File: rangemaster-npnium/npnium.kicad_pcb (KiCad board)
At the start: 2 copper layers, 40 x 44 mm, 26 parts, among them J1 Conn_01x07_Male, Q1 Q_NPN_CBE

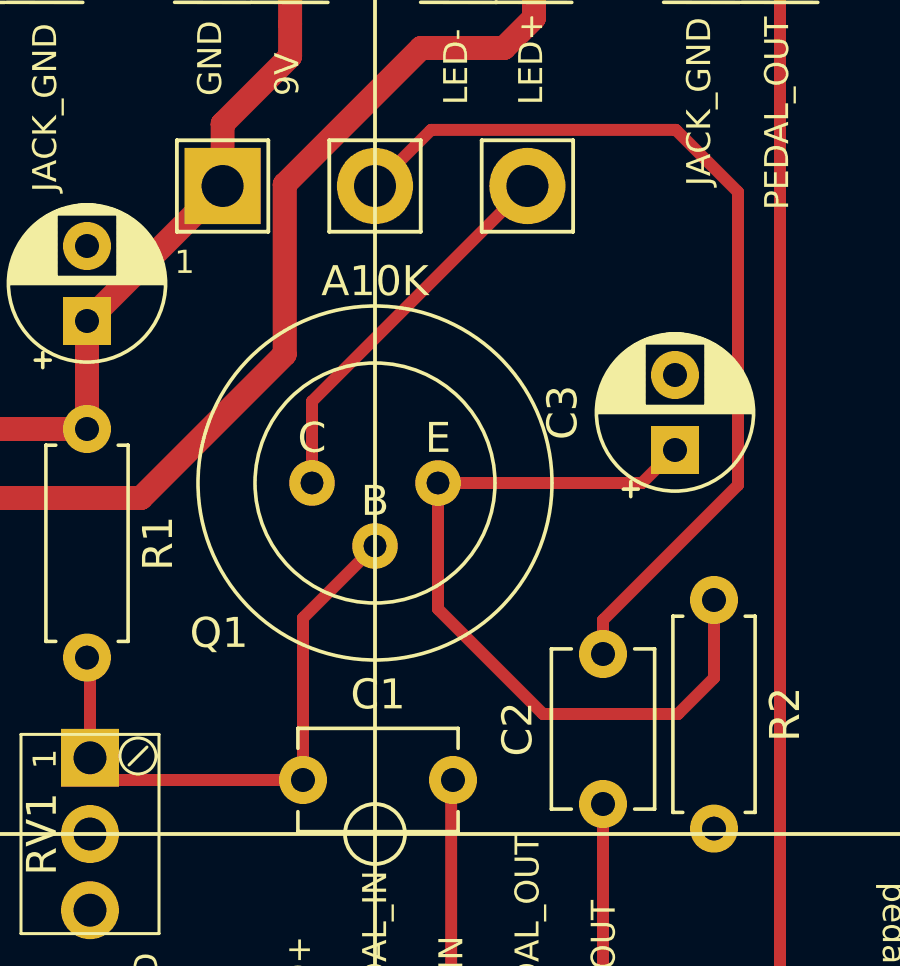
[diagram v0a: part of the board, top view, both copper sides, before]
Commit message: Migrating transistor footprint
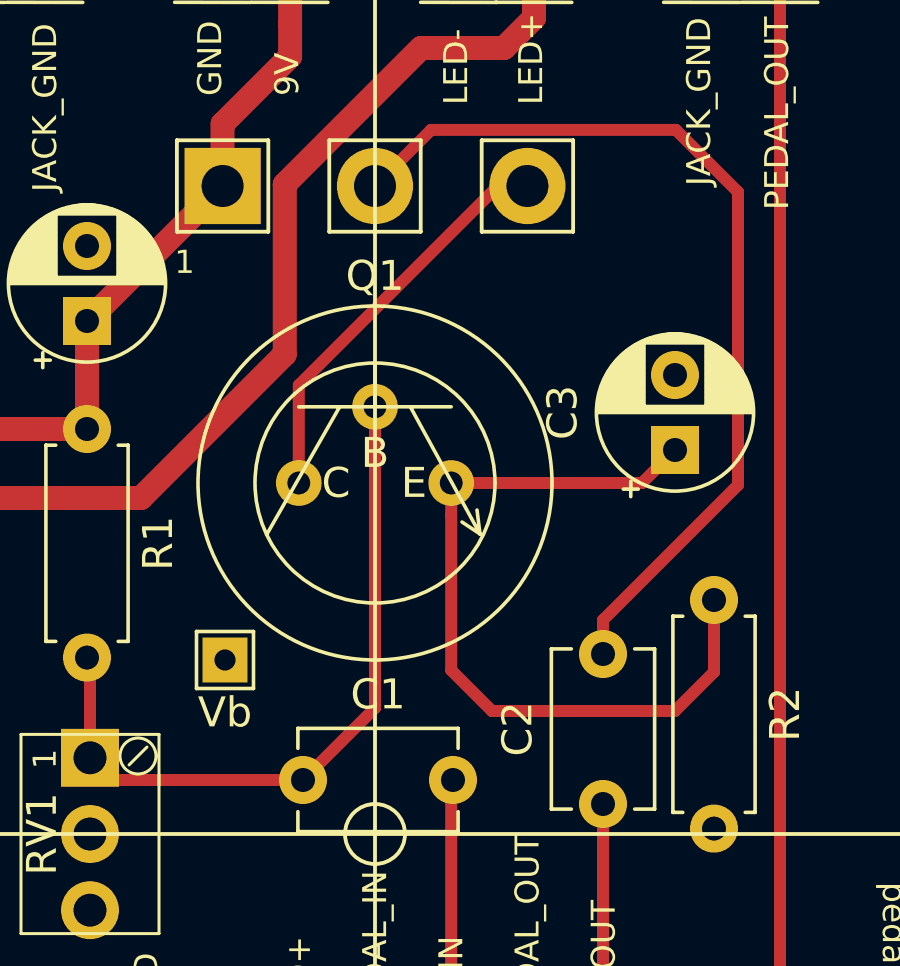
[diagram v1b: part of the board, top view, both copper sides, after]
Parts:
- added TP1: Vb, TestPoint:TestPoint_THTPad_1.5x1.5mm_Drill0.7mm, F.Cu at (95.0, 94.2)
- Q1: footprint pedal-component-footprint:Transistor_KTYU-3-6_CBE_d11.7mm -> pedal-component-footprint:Transistor_TO-5_CBE_d10.1mm
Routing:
- net Net-(C1-Pad1): track 19.6 -> 24.2 mm
- net Net-(Q1-Pad1): track 12.9 -> 13.6 mm
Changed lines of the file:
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@@
     (thickness 1.6)
     (drawings 10)
-    (tracks 66)
+    (tracks 67)
     (zones 0)
-    (modules 26)
+    (modules 27)
     (nets 12)
   )
@@
     (add_net "Net-(H6-Pad1)")
   )
+  (module TestPoint:TestPoint_THTPad_1.5x1.5mm_Drill0.7mm (layer F.Cu)
+    (at 95 94.2)
+    (descr "THT rectangular pad as test Point, square 1.5mm side length, hole diameter 0.7mm")
+    (tags "test point THT pad rectangle square")
+    (attr virtual)
+    (fp_text reference TP1 (at 0 -1.648) (layer F.SilkS) hide
+      (effects (font (size 1 1) (thickness 0.15)))
+    )
+    (fp_text value Vb (at 0 1.75) (layer F.SilkS)
+      (effects (font (size 1 1) (thickness 0.15)))
+    )
+    (fp_line (start 1.25 1.25) (end -1.25 1.25) (layer F.CrtYd) (width 0.05))
+    (fp_line (start 1.25 1.25) (end 1.25 -1.25) (layer F.CrtYd) (width 0.05))
+    (fp_line (start -1.25 -1.25) (end -1.25 1.25) (layer F.CrtYd) (width 0.05))
+    (fp_line (start -1.25 -1.25) (end 1.25 -1.25) (layer F.CrtYd) (width 0.05))
+    (fp_line (start -0.95 0.95) (end -0.95 -0.95) (layer F.SilkS) (width 0.12))
+    (fp_line (start 0.95 0.95) (end -0.95 0.95) (layer F.SilkS) (width 0.12))
+    (fp_line (start 0.95 -0.95) (end 0.95 0.95) (layer F.SilkS) (width 0.12))
+    (fp_line (start -0.95 -0.95) (end 0.95 -0.95) (layer F.SilkS) (width 0.12))
+    (fp_text user %R (at 0 -1.65) (layer F.Fab)
+      (effects (font (size 1 1) (thickness 0.15)))
+    )
+    (pad 1 thru_hole rect (at 0 0) (size 1.5 1.5) (drill 0.7) (layers *.Cu *.Mask)
+      (net 3 "Net-(C1-Pad1)"))
+  )
   (module "MBv3 enclosures:125B" (layer F.Cu)
     (at 100 100)
@@
     (fp_line (start 26 57.5) (end 0 57.5) (layer F.SilkS) (width 0.127))
   )
+  (module pedal-component-footprint:Transistor_TO-5_CBE_d10.1mm (layer F.Cu)
+    (at 100 88.3)
+    (fp_text reference Q1 (at 0 -6.9) (layer F.SilkS)
+      (effects (font (size 1 1) (thickness 0.15)))
+    )
+    (fp_text value Q_NPN_CBE (at 0 -6.8) (layer F.Fab)
+      (effects (font (size 1 1) (thickness 0.15)))
+    )
+    (fp_circle (center 0 0) (end 0 5.9) (layer F.SilkS) (width 0.12))
+    (fp_circle (center 0 0) (end 0 4) (layer F.SilkS) (width 0.12))
+    (fp_text user C (at -1.3 0) (layer F.SilkS)
+      (effects (font (size 1 1) (thickness 0.15)))
+    )
+    (fp_text user E (at 1.3 0) (layer F.SilkS)
+      (effects (font (size 1 1) (thickness 0.15)))
+    )
+    (fp_text user B (at 0 -1) (layer F.SilkS)
+      (effects (font (size 1 1) (thickness 0.15)))
+    )
+    (fp_line (start -2.54 -2.54) (end 2.54 -2.54) (layer F.SilkS) (width 0.12))
+    (fp_line (start -1.2 -2.5) (end -3.6 1.7) (layer F.SilkS) (width 0.12))
+    (fp_line (start 1.2 -2.5) (end 3.5 1.7) (layer F.SilkS) (width 0.12))
+    (fp_line (start 0 -2.6) (end 0 -4) (layer F.SilkS) (width 0.12))
+    (fp_line (start 3.5 1.7) (end 3.4 0.9) (layer F.SilkS) (width 0.12))
+    (fp_line (start 3.5 1.7) (end 2.9 1.3) (layer F.SilkS) (width 0.12))
+    (pad 1 thru_hole circle (at -2.54 0) (size 1.524 1.524) (drill 0.762) (layers *.Cu *.Mask)
+      (net 11 "Net-(Q1-Pad1)"))
+    (pad 2 thru_hole circle (at 0 -2.54) (size 1.524 1.524) (drill 0.762) (layers *.Cu *.Mask)
+      (net 3 "Net-(C1-Pad1)"))
+    (pad 3 thru_hole circle (at 2.54 0) (size 1.524 1.524) (drill 0.762) (layers *.Cu *.Mask)
+      (net 6 "Net-(C3-Pad1)"))
+  )
   (module pedal-component-footprint:PinHeader_1x01_P2.54mm_Long_Front_Back (layer F.Cu)
     (at 97.17 70.7)
@@
       (effects (font (size 1.2065 1.2065) (thickness 0.1524)) (justify mirror))
     )
-    (fp_text value A10K (at 0 -3.175) (layer F.SilkS)
+    (fp_text value A10K (at 0 2.9) (layer F.SilkS) hide
       (effects (font (size 1 1) (thickness 0.15)))
     )
@@
       (rotate (xyz 0 0 0))
     )
-  )
-  (module pedal-component-footprint:Transistor_KTYU-3-6_CBE_d11.7mm (layer F.Cu)
-    (at 100 88.3)
-    (fp_text reference Q1 (at -5.2 5) (layer F.SilkS)
-      (effects (font (size 1 1) (thickness 0.15)))
-    )
-    (fp_text value Q_NPN_CBE (at 0 -6.8) (layer F.Fab)
-      (effects (font (size 1 1) (thickness 0.15)))
-    )
-    (fp_text user E (at 2.1 -1.5) (layer F.SilkS)
-      (effects (font (size 1 1) (thickness 0.15)))
-    )
-    (fp_text user B (at 0 0.6) (layer F.SilkS)
-      (effects (font (size 1 1) (thickness 0.15)))
-    )
-    (fp_text user C (at -2.1 -1.5) (layer F.SilkS)
-      (effects (font (size 1 1) (thickness 0.15)))
-    )
-    (fp_circle (center 0 0) (end 0 5.9) (layer F.SilkS) (width 0.12))
-    (fp_circle (center 0 0) (end 0 4) (layer F.SilkS) (width 0.12))
-    (pad 1 thru_hole circle (at -2.1 0) (size 1.524 1.524) (drill 0.762) (layers *.Cu *.Mask)
-      (net 11 "Net-(Q1-Pad1)"))
-    (pad 2 thru_hole circle (at 0 2.1) (size 1.524 1.524) (drill 0.762) (layers *.Cu *.Mask)
-      (net 3 "Net-(C1-Pad1)"))
-    (pad 3 thru_hole circle (at 2.1 0) (size 1.524 1.524) (drill 0.762) (layers *.Cu *.Mask)
-      (net 6 "Net-(C3-Pad1)"))
   )
   (module pedal-component-footprint:BoardHeader_1x07_P2.54mm_Long_FXSide (layer F.Cu)
@@
   (segment (start 90.5 94.22) (end 90.4 94.12) (width 0.4) (layer F.Cu) (net 3))
   (segment (start 90.5 97.46) (end 90.5 94.22) (width 0.4) (layer F.Cu) (net 3))
-  (segment (start 97.6 92.8) (end 100 90.4) (width 0.4) (layer F.Cu) (net 3))
-  (segment (start 97.6 98.2) (end 97.6 92.8) (width 0.4) (layer F.Cu) (net 3))
+  (segment (start 100 95.8) (end 100 85.76) (width 0.4) (layer F.Cu) (net 3))
+  (segment (start 97.6 98.2) (end 100 95.8) (width 0.4) (layer F.Cu) (net 3))
   (segment (start 107.6 92.86863) (end 107.6 94) (width 0.4) (layer F.Cu) (net 4))
   (segment (start 112.1 78.6) (end 112.1 88.36863) (width 0.4) (layer F.Cu) (net 4))
@@
   (segment (start 107.6 99) (end 107.6 108.48) (width 0.4) (layer F.Cu) (net 5))
   (segment (start 108.9 88.3) (end 110 87.2) (width 0.4) (layer F.Cu) (net 6))
-  (segment (start 102.1 88.3) (end 108.9 88.3) (width 0.4) (layer F.Cu) (net 6))
-  (segment (start 102.1 92.5) (end 102.1 89.37763) (width 0.4) (layer F.Cu) (net 6))
-  (segment (start 105.6 96) (end 102.1 92.5) (width 0.4) (layer F.Cu) (net 6))
-  (segment (start 110.1 96) (end 105.6 96) (width 0.4) (layer F.Cu) (net 6))
-  (segment (start 102.1 89.37763) (end 102.1 88.3) (width 0.4) (layer F.Cu) (net 6))
-  (segment (start 111.3 94.8) (end 110.1 96) (width 0.4) (layer F.Cu) (net 6))
-  (segment (start 111.3 92.2) (end 111.3 94.8) (width 0.4) (layer F.Cu) (net 6))
+  (segment (start 102.54 88.3) (end 108.9 88.3) (width 0.4) (layer F.Cu) (net 6))
+  (segment (start 102.54 94.54) (end 102.54 89.37763) (width 0.4) (layer F.Cu) (net 6))
+  (segment (start 103.9 95.9) (end 102.54 94.54) (width 0.4) (layer F.Cu) (net 6))
+  (segment (start 102.54 89.37763) (end 102.54 88.3) (width 0.4) (layer F.Cu) (net 6))
+  (segment (start 111.3 92.2) (end 111.3 94.6) (width 0.4) (layer F.Cu) (net 6))
+  (segment (start 110 95.9) (end 103.9 95.9) (width 0.4) (layer F.Cu) (net 6))
+  (segment (start 111.3 94.6) (end 110 95.9) (width 0.4) (layer F.Cu) (net 6))
   (segment (start 97.17 73) (end 97.17 70.7) (width 0.8) (layer F.Cu) (net 7))
   (segment (start 97.17 74.08) (end 97.17 73) (width 0.8) (layer F.Cu) (net 7))
@@
   (segment (start 104.3 73.8) (end 101.536398 73.8) (width 0.8) (layer F.Cu) (net 10))
   (segment (start 105.3 72.8) (end 104.3 73.8) (width 0.8) (layer F.Cu) (net 10))
-  (segment (start 97.9 85.58) (end 105.08 78.4) (width 0.4) (layer F.Cu) (net 11))
-  (segment (start 97.9 88.3) (end 97.9 85.58) (width 0.4) (layer F.Cu) (net 11))
+  (segment (start 104.1 78.4) (end 105.08 78.4) (width 0.4) (layer F.Cu) (net 11))
+  (segment (start 97.46 85.04) (end 104.1 78.4) (width 0.4) (layer F.Cu) (net 11))
+  (segment (start 97.46 88.3) (end 97.46 85.04) (width 0.4) (layer F.Cu) (net 11))
   (zone (net 1) (net_name GND) (layer B.Cu) (hatch edge 0.508)
     (connect_pads (clearance 0.508))

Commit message: wip
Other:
- net class Default removed
- net class PWR removed
